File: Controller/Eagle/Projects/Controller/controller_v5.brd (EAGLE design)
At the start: 250 x 115 mm, 71 parts, among them J2 AVR_SPI_PRG_6NS, J3 GIMBAL_3PIN, J4 GIMBAL_3PIN, J5 GIMBAL_3PIN, J6 GIMBAL_3PIN, U2 ATMEGA128RFA1, U3 RF_AMPLIFIER, Y1 32.768kHz, Y2 16MHz

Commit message: Adding v5 of the controller board, which only has one antenna
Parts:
- removed C11, C4, C9: 2.2 pF, Controller:0805
- removed C3: TODO, Controller:0805
- removed J$1: SMA_EDGE, Controller:SMA-EDGE
- removed L1: 1.8 nH, Controller:0805
- removed L2: 1 nH, Controller:0805
- removed L3: 4.7 nH, Controller:0805
- removed R16: 10K, SparkFun:3386U
- removed R4: 3.9K, Controller:0805
- removed SJ1, SJ2: SOLDERJUMPERTRACE, Controller:SJ_2S-TRACE
- removed SJ3, SJ4: SOLDERJUMPERNC, Controller:SJ_2S
- removed U3: RF_AMPLIFIER, Controller:QFN65P400X400X100-17N
- added R1: 10K, Controller:3386U
- moved R14 22.8 mm to (229.0, 103.4)
- moved R13 21.5 mm to (229.0, 18.4), turned to 90 degrees
- moved U$7 17.1 mm to (80.0, 100.0)
- moved U$5 13.1 mm to (56.9, 92.7), turned to 0 degrees
- moved D1 12.2 mm to (52.5, 100.0), turned to 270 degrees
- moved S1 10.5 mm to (98.6, 72.3)
- moved Y1 8.89 mm to (96.9, 84.9), turned to 90 degrees
- moved JP5 8.75 mm to (90.0, 110.0)
- moved R17 8.61 mm to (62.0, 89.7)
- moved JP2 8.48 mm to (55.5, 88.5)
- moved C15 8.32 mm to (124.0, 26.9)
- moved LED2 8.11 mm to (61.9, 104.0)
- moved C14 7.00 mm to (118.9, 27.9)
- moved C19 6.79 mm to (99.9, 86.2), turned to 0 degrees
- moved A1 6.71 mm to (125.0, 109.3), flipped to the top
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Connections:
- removed net N$1: C9.1, L1.2, L2.1
- removed net N$13: C1.1, SJ3.2
- removed net N$14: C2.1, SJ4.2
- removed net N$17: SJ2.1, U3.3
- removed net N$3: C11.1, L2.2, L3.2, U3.10
- removed net N$4: C3.2, C4.1, L1.1
- removed net N$6: SJ1.1, U3.2
- removed net N$7: R4.1, U3.8
- removed net N$8: C3.1, J$1.SIG
- removed net TST: U2.11
- net 3.3V: no longer L3.1, U3.13, U3.14, U3.15
- net ADC4/GM_SEL: no longer U3.7
- net ADC5/LNA_EN: no longer U3.6
- net ADC6/PA_EN: no longer U3.5
- net GND: now also R1.3, U2.11; no longer C11.2, C4.2, C9.2, R16.3, R4.2, U3.1, U3.11, U3.12, U3.16, U3.4, U3.9, U3.PAD
- net N$10: now also C2.1; no longer SJ4.1
- net N$9: now also C1.1; no longer SJ3.1
- net RF_N: no longer SJ1.2
- net RF_P: no longer SJ2.2
- net VCC: now also R1.1; no longer R16.1
- net VCUTOFF: now also R1.2; no longer R16.2
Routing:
- net GND: track 959.7 -> 1358.1 mm, vias 15 -> 11
- net 3.3V: track 1037.0 -> 1260.9 mm, vias 10 -> 4
- net RESET_N: track 78.6 -> 122.8 mm
- net VCC: track 100.4 -> 61.2 mm
- net PE7: track 102.9 -> 126.0 mm, vias 4 -> 0
- net PE6: track 115.7 -> 136.6 mm, vias 4 -> 0
- net ADC0: track 65.6 -> 82.5 mm, vias 2 -> 1
- net ADC4/GM_SEL: track 14.3 -> 0.00 mm
- net PD0/I2C_SCL: track 72.5 -> 86.2 mm
- net ADC5/LNA_EN: track 13.4 -> 0.00 mm
- net ADC6/PA_EN: track 12.6 -> 0.00 mm
- net N$3: track 12.0 -> 0.00 mm
- net N$1: track 11.9 -> 0.00 mm
- net ADC2: track 64.0 -> 73.1 mm
- net N$20: track 25.6 -> 16.5 mm
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
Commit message: In the controller, finished connecting unconnected pins and Passed DRC using the Seeedstudio DRC files.
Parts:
- added JP1, JP6: (no value), Controller:1X04
- added R16, R18, R19, R2, R20, R21, R22, R23, R3, R4: 10 k, Controller:0805
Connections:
- removed net ADC4/GM_SEL: U2.3
- removed net ADC5/LNA_EN: U2.4
- removed net ADC6/PA_EN: U2.5
- removed net GM_SEL: U2.14
- removed net LNA_EN: U2.15
- removed net PA_EN: U2.16
- new net ADC4: JP1.4, U2.3
- new net ADC5: JP1.3, U2.4
- new net ADC6: JP1.2, U2.5
- new net PB0: R22.2, U2.36
- new net PB1: R23.2, U2.19
- new net PG0: JP6.2, U2.14
- new net PG1: JP6.3, U2.15
- new net PG2: JP6.4, U2.16
- new net RESET_OUT: JP6.1, U2.13
- net ADC7: now also JP1.1
- net GND: now also R16.1, R18.1, R19.1, R2.1, R20.1, R21.1, R22.1, R23.1, R3.1, R4.1, U2.10, U2.7
- net PD4: now also R18.2
- net PD5: now also R19.2
- net PD6: now also R21.2
- net PD7: now also R20.2
- net PE2: now also R2.2
- net PE3: now also R3.2
- net PE4: now also R4.2
- net PE5: now also R16.2
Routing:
- net GND: track 1358.1 -> 1415.9 mm, vias 11 -> 15
- net ADC4: track 0.00 -> 26.4 mm
- net ADC5: track 0.00 -> 24.7 mm
- net ADC6: track 0.00 -> 22.4 mm, vias 0 -> 1
- net PG2: track 0.00 -> 19.6 mm
- net ADC7: track 0.00 -> 19.3 mm
- net PG1: track 0.00 -> 19.1 mm
- net PG0: track 0.00 -> 18.3 mm
- net PB1: track 0.00 -> 12.0 mm
- net RESET_OUT: track 0.00 -> 11.8 mm
- net PE5: track 0.00 -> 10.3 mm
- net PD4: track 0.00 -> 10.0 mm
- net PB0: track 0.00 -> 9.68 mm
- net PE4: track 0.00 -> 8.08 mm
- net PD5: track 0.00 -> 8.00 mm
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
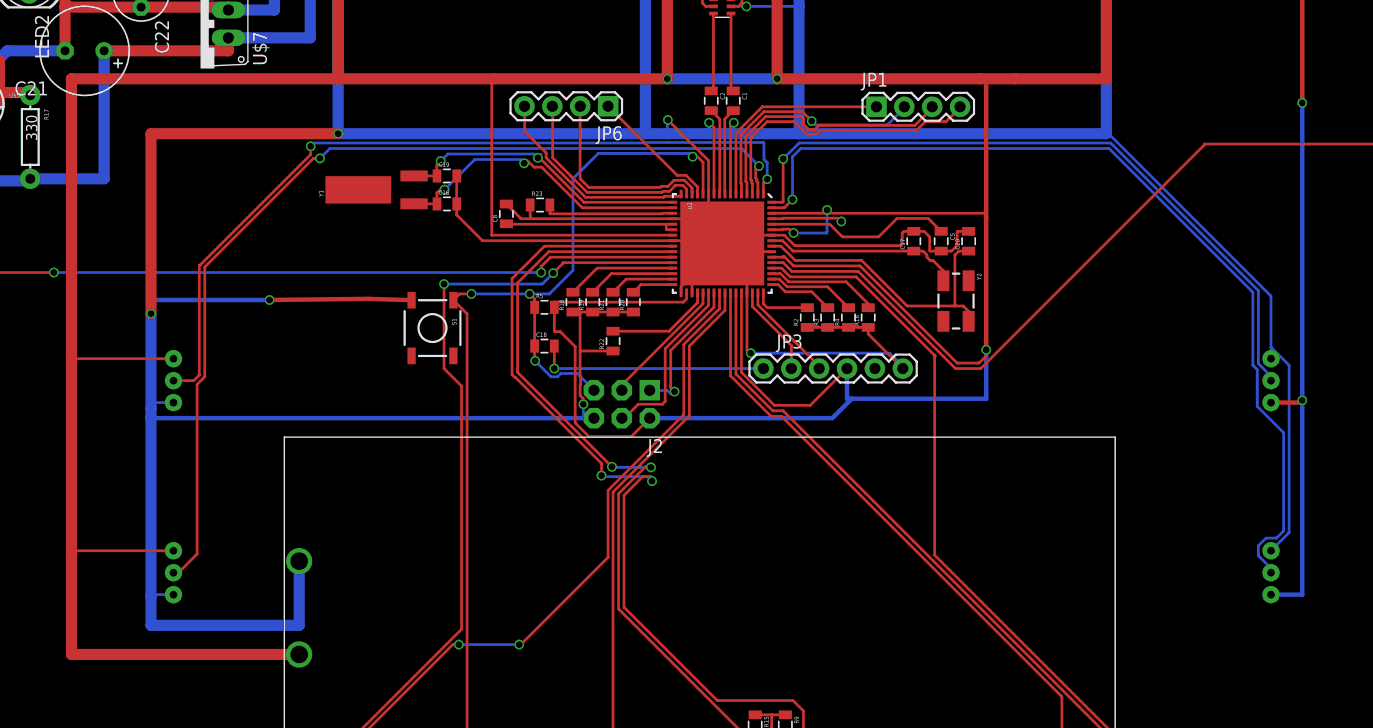
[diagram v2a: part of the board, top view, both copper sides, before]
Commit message: Added additional resistors to the gimbals to create a resistor ladder and meet the ADC swing voltage requirements.
Also, cleaned up some of the board routing.
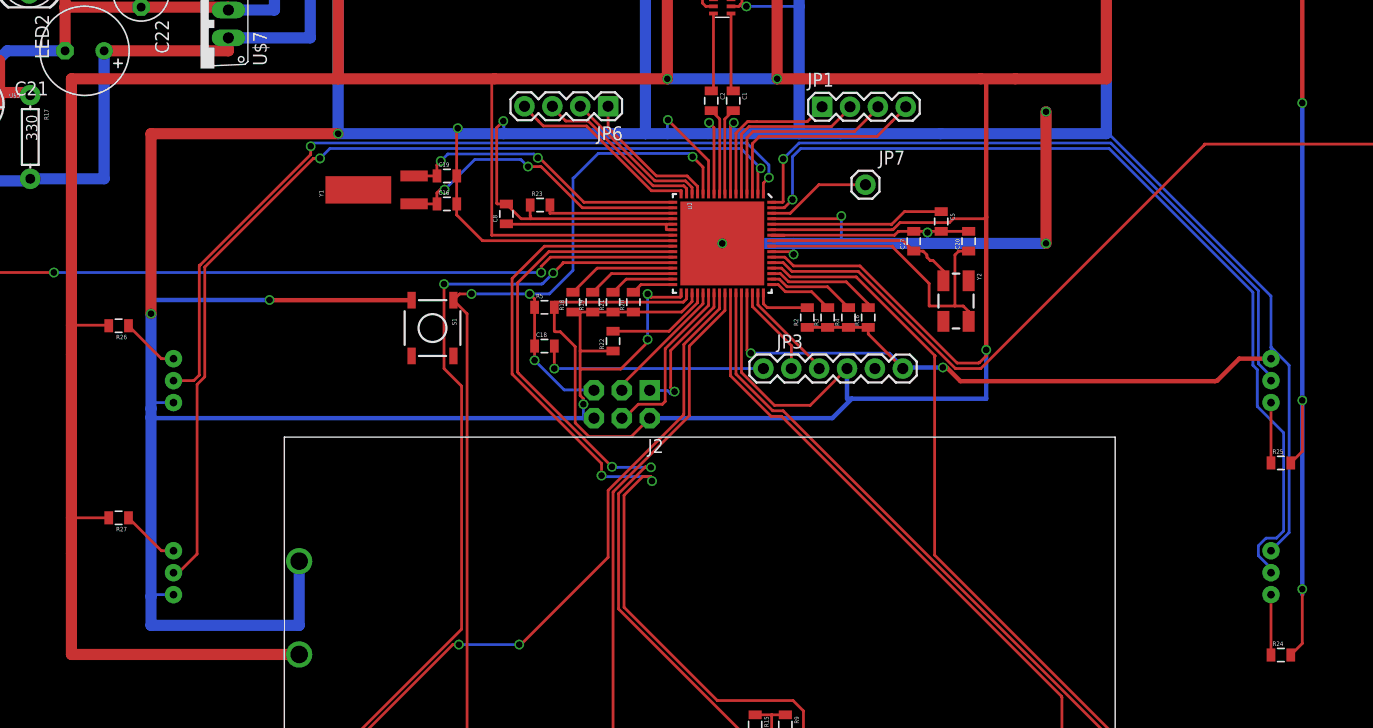
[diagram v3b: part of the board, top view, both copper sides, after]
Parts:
- added JP7: M01PTH, Controller:1X01
- added R24, R25, R26, R27: 5K, Controller:0805
- moved JP1 4.95 mm to (134.1, 92.5)
- moved C5 1.80 mm to (144.9, 82.0)
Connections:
- new net AREF: JP7.1, U2.62
- new net N$1: J6.1, R24.1
- new net N$3: J3.1, R25.1
- new net N$4: J5.1, R26.1
- new net N$6: J4.1, R27.1
- net 3.3V: now also R24.2, R25.2, R26.2, R27.2; no longer J3.1, J4.1, J5.1, J6.1, U2.62
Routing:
- net GND: track 1415.9 -> 1505.1 mm, vias 15 -> 25
- net 3.3V: track 1265.8 -> 1253.6 mm, vias 7 -> 6
- net AREF: track 0.00 -> 9.63 mm
- net ADC4: track 26.4 -> 20.0 mm
- net ADC5: track 24.7 -> 18.3 mm
- net ADC6: track 22.4 -> 16.5 mm, vias 1 -> 0
- net N$3: track 0.00 -> 5.50 mm
- net N$1: track 0.00 -> 5.50 mm
- net N$6: track 0.00 -> 5.34 mm
- net N$4: track 0.00 -> 5.34 mm
- net ADC7: track 19.3 -> 14.4 mm
- net PG0: track 18.3 -> 13.9 mm
- net PG1: track 19.1 -> 15.9 mm
- net PG2: track 19.6 -> 17.8 mm
- net XTAL2_16MHZ: track 27.4 -> 28.6 mm
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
